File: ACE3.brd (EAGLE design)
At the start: 100 x 80 mm, 140 parts, among them IC1 7805T, Q1 2N3904, Q2 2N3904, Q3 BC237, X1 6M5

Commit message: Correct problem the CNT8 as input for Video Screen Access.
Signed-off-by: John Bradley <flypie@rocketmail.com>
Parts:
- S1: value (none) -> 1
- S10: value (none) -> 0
- S11: value (none) -> Q
- S12: value (none) -> W
- S13: value (none) -> E
- S14: value (none) -> R
- S15: value (none) -> T
- S16: value (none) -> Y
- S17: value (none) -> U
- S18, S27: value (none) -> I
- S19: value (none) -> O
- S2: value (none) -> 2
- S20: value (none) -> P
- S21: value (none) -> A
- S22: value (none) -> S
- S23: value (none) -> D
- S24: value (none) -> F
- S25: value (none) -> G
- S26: value (none) -> H
- S28: value (none) -> J
- S29: value (none) -> K
- S3: value (none) -> 3
- S30: value (none) -> L
- S31: value (none) -> SHIFT
- S32: value (none) -> CTRL
- S33: value (none) -> Z
- S34: value (none) -> X
- S35: value (none) -> C
- S36: value (none) -> V
- S37: value (none) -> B
- S38: value (none) -> N
- S39: value (none) -> M
- S4: value (none) -> 4
- S40: value (none) -> SPACE
- S5: value (none) -> 5
- S6: value (none) -> 6
- S7: value (none) -> 7
- S8: value (none) -> 8
- S9: value (none) -> 9
- moved Z51 1198.0 mm to (-22.9, 109.2)
- moved Z5-6 1179.4 mm to (-27.9, 59.7)
- moved Z50 1131.1 mm to (-144.8, 97.8)
- moved Z52 1111.8 mm to (-109.2, 40.6)
- moved E1 1108.5 mm to (-68.6, 109.2)
- moved R23 1107.5 mm to (-142.2, 158.8)
- moved R22 1103.8 mm to (-135.9, 158.8)
- moved E2 1103.7 mm to (-116.8, 106.7)
- moved R21 1100.2 mm to (-129.5, 158.8)
- moved R20 1096.6 mm to (-123.2, 158.8)
- moved R19 1093.1 mm to (-116.8, 158.8)
- moved RN2 1092.8 mm to (-24.1, 74.9)
- moved R11 1092.4 mm to (-22.9, 165.1)
- moved R18 1089.7 mm to (-110.5, 158.8)
- moved Z3-4 1087.7 mm to (-71.1, 40.6)
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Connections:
- net CNT12: now also R16.1; no longer R15.1
- net CNT13: now also R17.1; no longer R16.1
- net CNT14: now also R18.1; no longer R17.1
- net CNT15: now also R19.1; no longer R18.1
- net CNT16: now also R20.1; no longer R19.1
- net CNT17: no longer R20.1
- net CNT7: now also R15.1

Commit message: Minor changes update  crystal.
Signed-off-by: John Bradley <flypie@rocketmail.com>
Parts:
- X1: value 6M5 -> 6.556MHz; device crystal:HC49GW -> crystal:HC49U-V
- moved S3 144.9 mm to (-148.6, 57.1)
- moved S17 142.0 mm to (-149.9, 76.2)
- moved S31 141.1 mm to (-149.9, 87.6)
- moved X1 136.8 mm to (-118.1, 142.2)
- moved C15 134.4 mm to (-16.5, 152.4)
- moved C16 134.4 mm to (-22.9, 152.4)
- moved Z22 124.0 mm to (-144.8, 120.7)
- moved Z51 124.0 mm to (-144.8, 132.1)
- moved Z29 116.6 mm to (-138.4, 109.2)
- moved RN2 115.3 mm to (-137.2, 97.8)
- moved S1 51.6 mm to (-128.3, 57.1)
- moved S2 51.6 mm to (-138.4, 57.1)
- moved RN1 46.0 mm to (-114.3, 97.8)
- moved S10 44.4 mm to (-78.7, 76.2)
- moved S16 44.4 mm to (-139.7, 76.2)
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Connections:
- net N$36: now also X1.1; no longer X1.2
- net N$47: now also X1.2; no longer X1.1

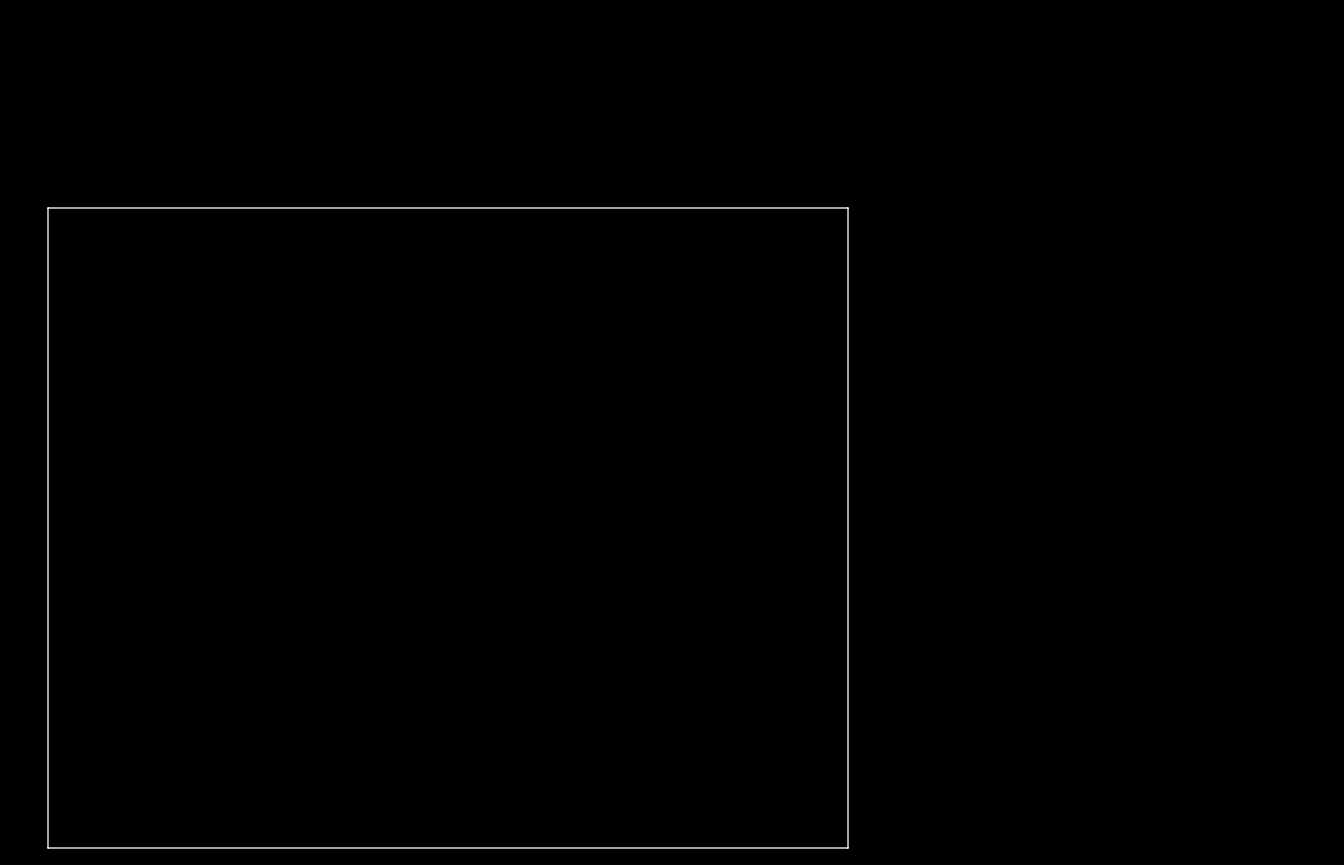
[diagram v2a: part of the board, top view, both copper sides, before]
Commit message: Add ACE2BOKB with a socket for a keyboard.
Signed-off-by: John Bradley <flypie@rocketmail.com>
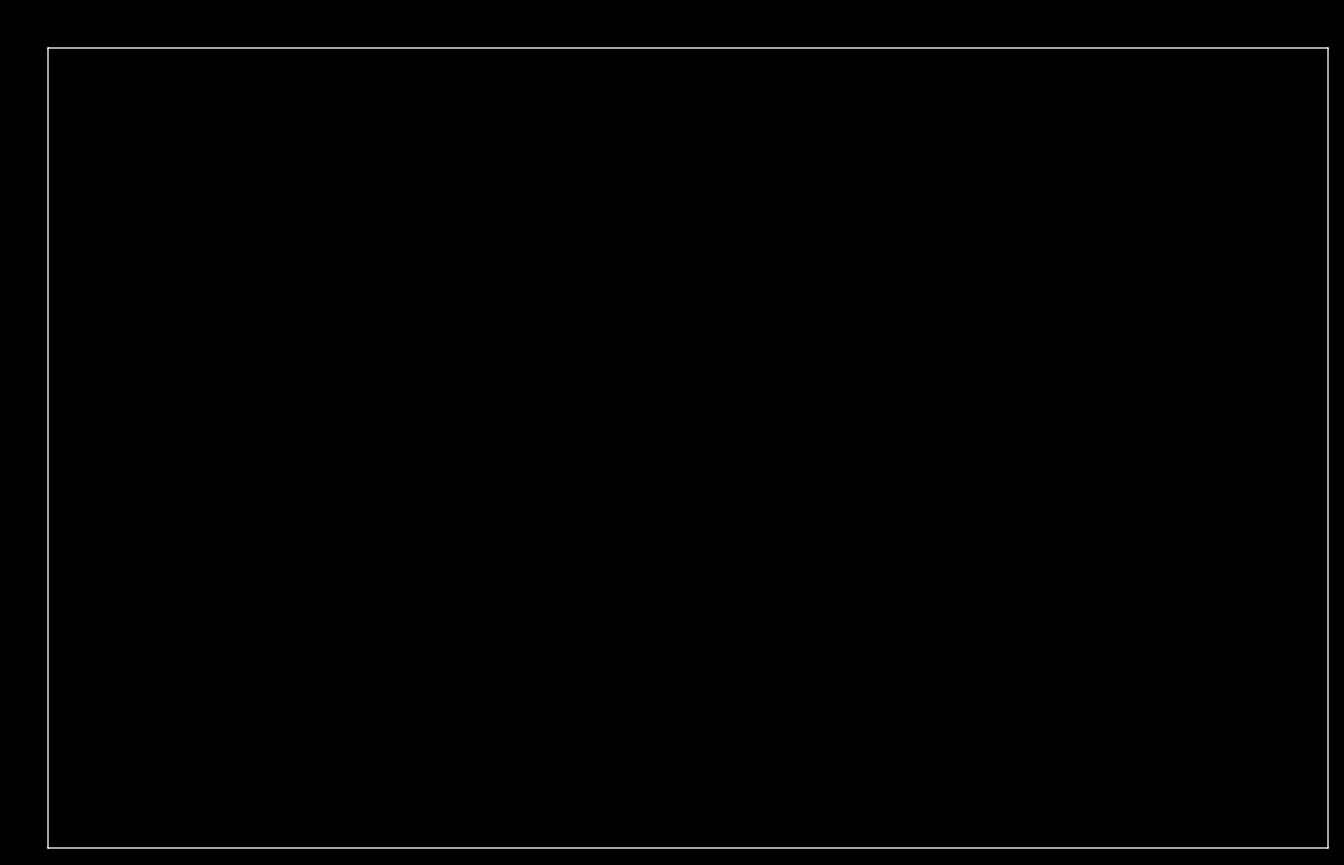
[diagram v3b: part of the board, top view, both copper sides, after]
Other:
- board size 100 x 80 mm -> 160 x 100 mm
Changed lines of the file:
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@@
 <layers>
 <layer number="1" name="Top" color="4" fill="1" visible="yes" active="yes"/>
+<layer number="2" name="Route2" color="16" fill="1" visible="no" active="no"/>
+<layer number="15" name="Route15" color="23" fill="1" visible="no" active="no"/>
 <layer number="16" name="Bottom" color="1" fill="1" visible="yes" active="yes"/>
 <layer number="17" name="Pads" color="2" fill="1" visible="yes" active="yes"/>
@@
 <board>
 <plain>
-<wire x1="0" y1="0" x2="100" y2="0" width="0" layer="20"/>
-<wire x1="100" y1="0" x2="100" y2="80" width="0" layer="20"/>
-<wire x1="100" y1="80" x2="0" y2="80" width="0" layer="20"/>
-<wire x1="0" y1="80" x2="0" y2="0" width="0" layer="20"/>
+<wire x1="0" y1="0" x2="160" y2="0" width="0" layer="20"/>
+<wire x1="160" y1="0" x2="160" y2="100" width="0" layer="20"/>
+<wire x1="160" y1="100" x2="0" y2="100" width="0" layer="20"/>
+<wire x1="0" y1="100" x2="0" y2="0" width="0" layer="20"/>
 </plain>
 <attributes>

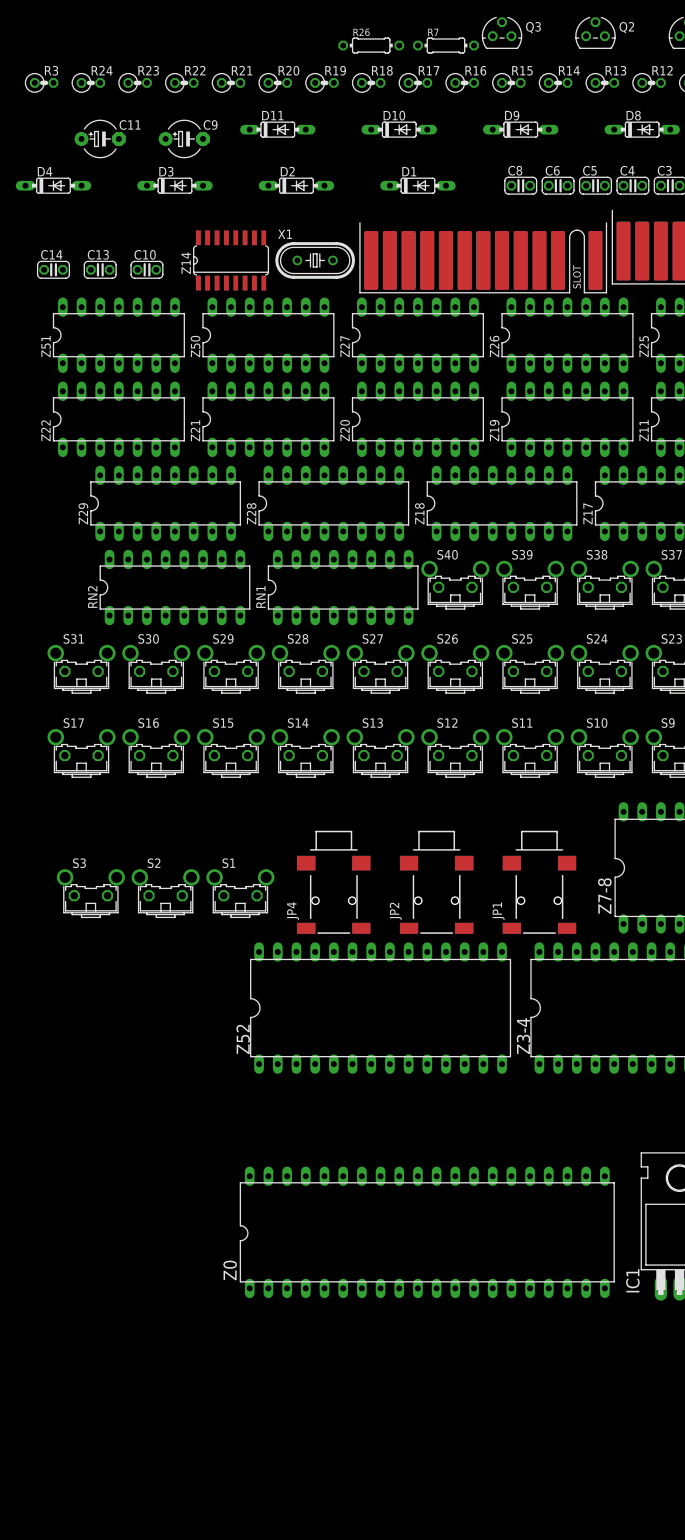
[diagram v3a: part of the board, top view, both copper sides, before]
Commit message: Update after faults pointed out by Claudius. Decoding address from 8k-16k changed. Transistor changed. Minor changed to take advantage of Hex Invert chip and remove cludged inverts.
Signed-off-by: John Bradley <flypie@rocketmail.com>
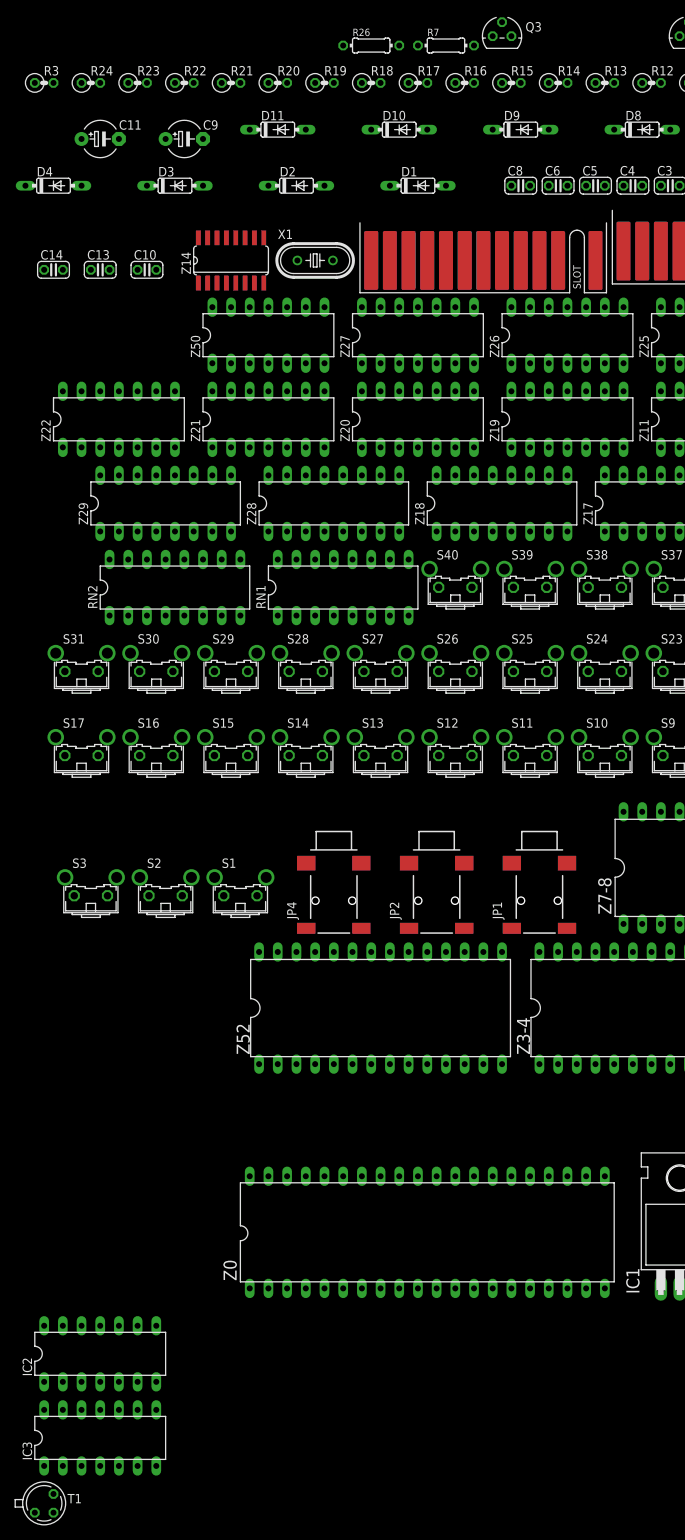
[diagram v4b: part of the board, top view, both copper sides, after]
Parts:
- removed Q2: 2N3904, transistor:TO92
- removed Z51: 74S00N, 74xx-eu:DIL14
- added IC2: 74HCT04N, 74xx-eu:DIL14
- added IC3: 74HCT08N, 74xx-eu:DIL14
- added T1: 2N2369, transistor:TO18
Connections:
- new net N$28: Z22.11, Z29.7
- new net N$30: IC2.2, IC3.1
- new net N$66: Z29.13, Z50.2
- net /INT: now also IC2.8; no longer Z19.11
- net ADDRESS12: now also IC2.1, IC3.4
- net CSB4KV: now also IC2.11; no longer Z23.4
- net GND: now also IC2.7, IC3.7, T1.1; no longer Q2.3, Z51.7
- net N$1: now also Z29.12, Z50.4; no longer Z29.13, Z50.1
- net N$2: now also IC3.3; no longer Z29.14
- net N$21: now also IC2.10; no longer Z23.6
- net N$23: now also Z29.10; no longer Z29.9
- net N$24: now also T1.3; no longer Q2.1
- net N$25: now also Z29.9; no longer Z29.7
- net N$26: now also T1.2; no longer Q2.2
- net N$29: now also IC2.5; no longer Z23.2
- net N$3: now also Z29.11, Z50.5; no longer Z29.12, Z50.2
- net N$39: now also IC2.6; no longer Z23.3
- net N$50: now also IC2.9; no longer Z19.12
- net N$6: now also IC3.2, IC3.5, Z29.14; no longer Z29.11, Z50.4
- net N$7: now also IC3.6, Z50.1; no longer Z29.10, Z50.5
- net N$8: now also IC2.3; no longer Z51.1, Z51.2
- net N$9: now also IC2.4; no longer Z51.3
- net VCC: now also IC2.14, IC3.14; no longer Z19.13, Z22.11, Z23.1, Z23.5, Z51.14
